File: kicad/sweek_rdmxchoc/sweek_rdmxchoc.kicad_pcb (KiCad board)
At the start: 2 copper layers, 124.6 x 107.6 mm, 60 parts, among them J1 Conn_01x04_Socket, J2 OLED_128x32, SW1 RotaryEncoder_Switch, U1 RP2040_Zero

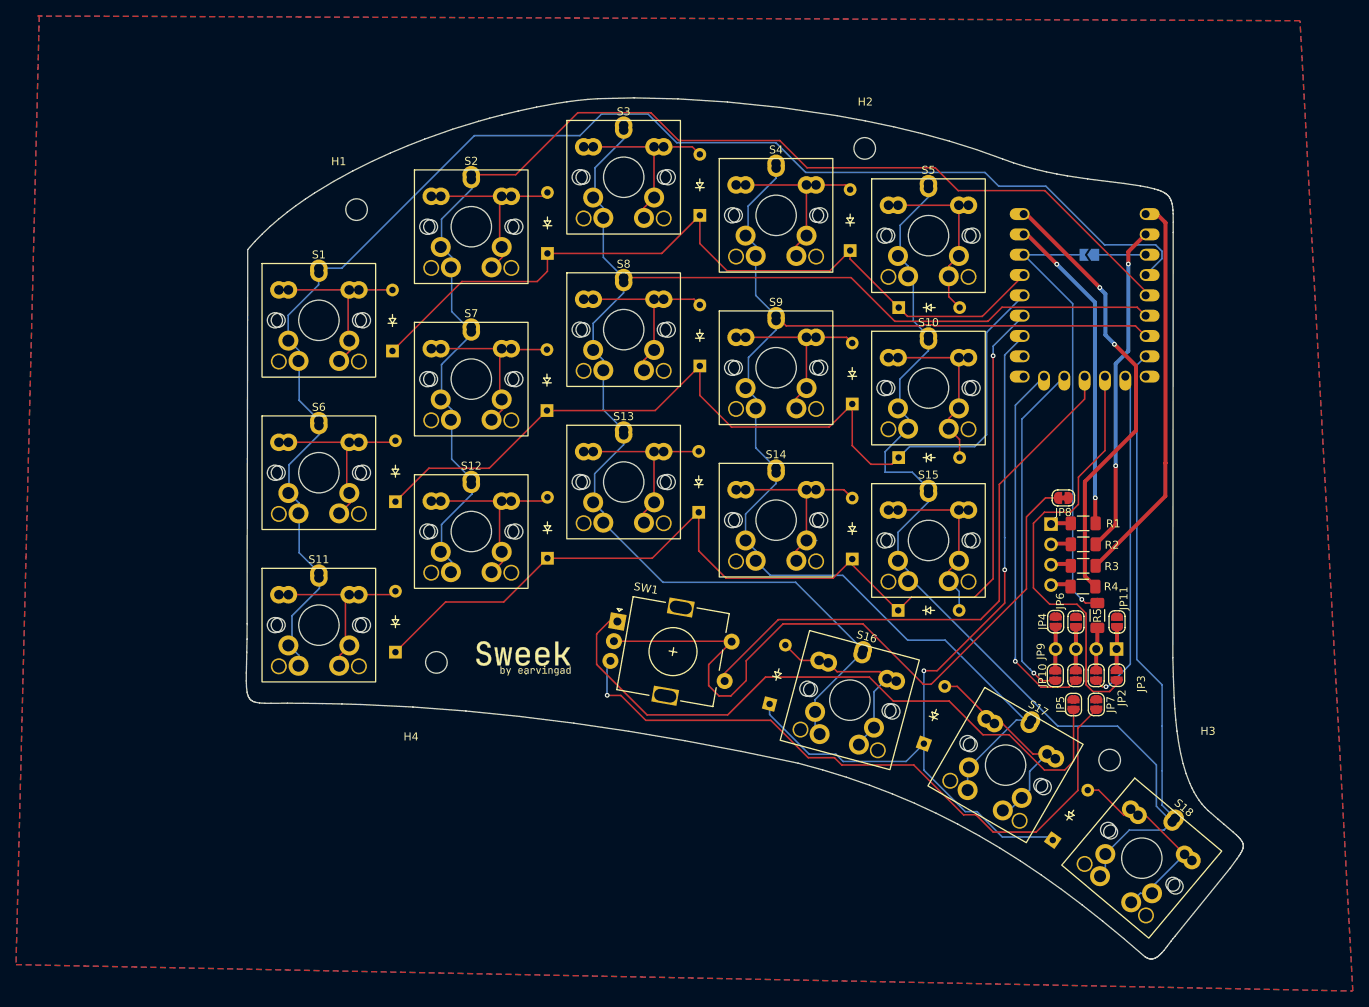
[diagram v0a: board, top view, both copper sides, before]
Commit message: Update sweek kicad files for v1.0.1
Update sweek kicad files for v1.0.1
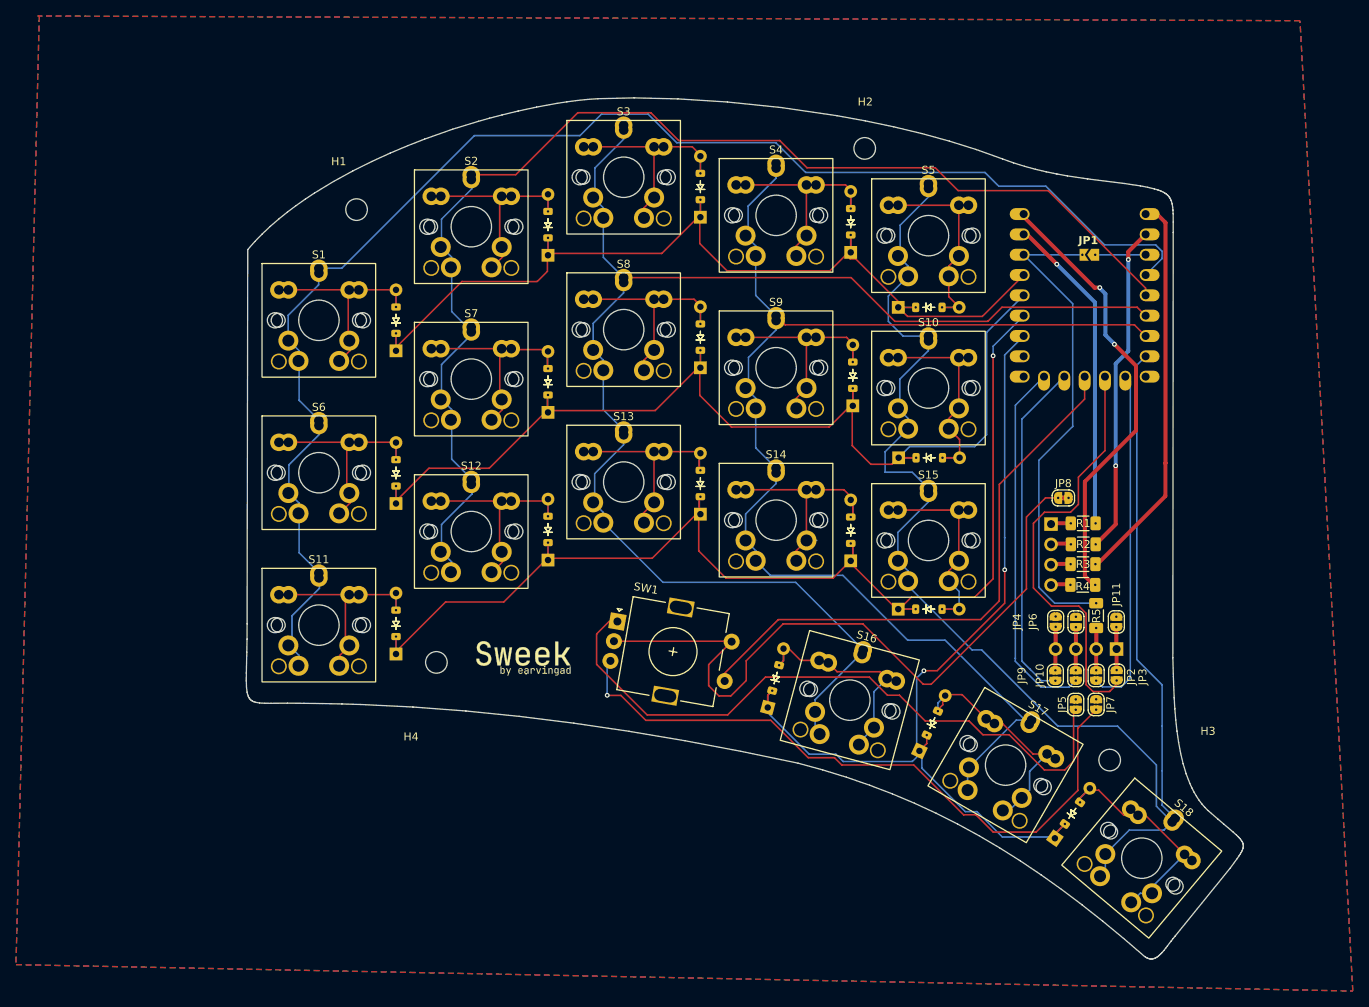
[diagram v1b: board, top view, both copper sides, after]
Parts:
- D1, D10, D11, D12, D13, D14, D15, D16, D17, D18, D2, D3, D4, D5, D6, D7, D8, D9: footprint ScottoKeebs_Components:Diode_DO-35 -> Redragon:Diode_DO-35_SOD-123
- JP1: footprint Jumper:SolderJumper-2_P1.3mm_Open_TrianglePad1.0x1.5mm -> Jumper:SolderJumper-2_P1.3mm_Open_TrianglePad1.0x1.5mm_custom
- JP10, JP11, JP2, JP3, JP4, JP5, JP6, JP7, JP9: footprint Jumper:SolderJumper-2_P1.3mm_Open_RoundedPad1.0x1.5mm -> Jumper:SolderJumper-2_P1.3mm_Open_RoundedPad1.0x1.5mm_custom
- JP8: footprint Jumper:SolderJumper-2_P1.3mm_Bridged_RoundedPad1.0x1.5mm -> Jumper:SolderJumper-2_P1.3mm_Bridged_RoundedPad1.0x1.5mm_custom
- R1, R2, R3, R4, R5: footprint Resistor_SMD:R_1206_3216Metric_Pad1.30x1.75mm_HandSolder -> Resistor_SMD:R_1206_3216Metric_Pad1.30x1.75mm_custom
- moved D18 4.23 mm to (119.7, 104.9)
- moved D1 3.93 mm to (35.1, 43.3)
- moved D15 3.90 mm to (101.8, 79.4)
- moved D10 3.89 mm to (101.8, 60.5)
- moved D5 3.83 mm to (101.8, 41.7)
- moved D13 3.67 mm to (73.1, 63.7)
- moved D14 3.66 mm to (91.9, 69.5)
- moved D7 3.66 mm to (54.1, 51.0)
- moved D4 3.66 mm to (91.9, 31.0)
- moved D9 3.66 mm to (92.2, 50.1)
- moved D2 3.66 mm to (54.1, 31.3)
- moved D3 3.66 mm to (73.1, 26.6)
- moved D11 3.66 mm to (35.1, 81.2)
- moved D12 3.66 mm to (54.1, 69.4)
- moved D6 3.66 mm to (35.1, 62.3)
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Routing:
- net Row2: track 128.4 -> 150.2 mm
- net Row1: track 114.8 -> 136.6 mm
- net Row0: track 99.4 -> 120.1 mm
- net Row3: track 104.1 -> 115.8 mm
- net VCC_33: track 56.3 -> 61.3 mm, vias 1 -> 0
- net Col4: track 185.3 -> 190.1 mm
- net Net-(D16-A): track 23.7 -> 28.3 mm
- net Net-(D18-A): track 25.0 -> 29.6 mm
- net Net-(D6-A): track 23.1 -> 27.4 mm
- net Net-(D9-A): track 23.0 -> 27.3 mm
- net Net-(D7-A): track 22.9 -> 27.2 mm
- net Net-(D2-A): track 23.1 -> 27.4 mm
- net Net-(D15-A): track 20.5 -> 24.8 mm
- net Net-(D14-A): track 23.3 -> 27.6 mm
- net Net-(D13-A): track 22.6 -> 26.9 mm
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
